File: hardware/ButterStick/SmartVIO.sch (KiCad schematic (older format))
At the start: 3 parts, among them U19 ATmega328PB-MU

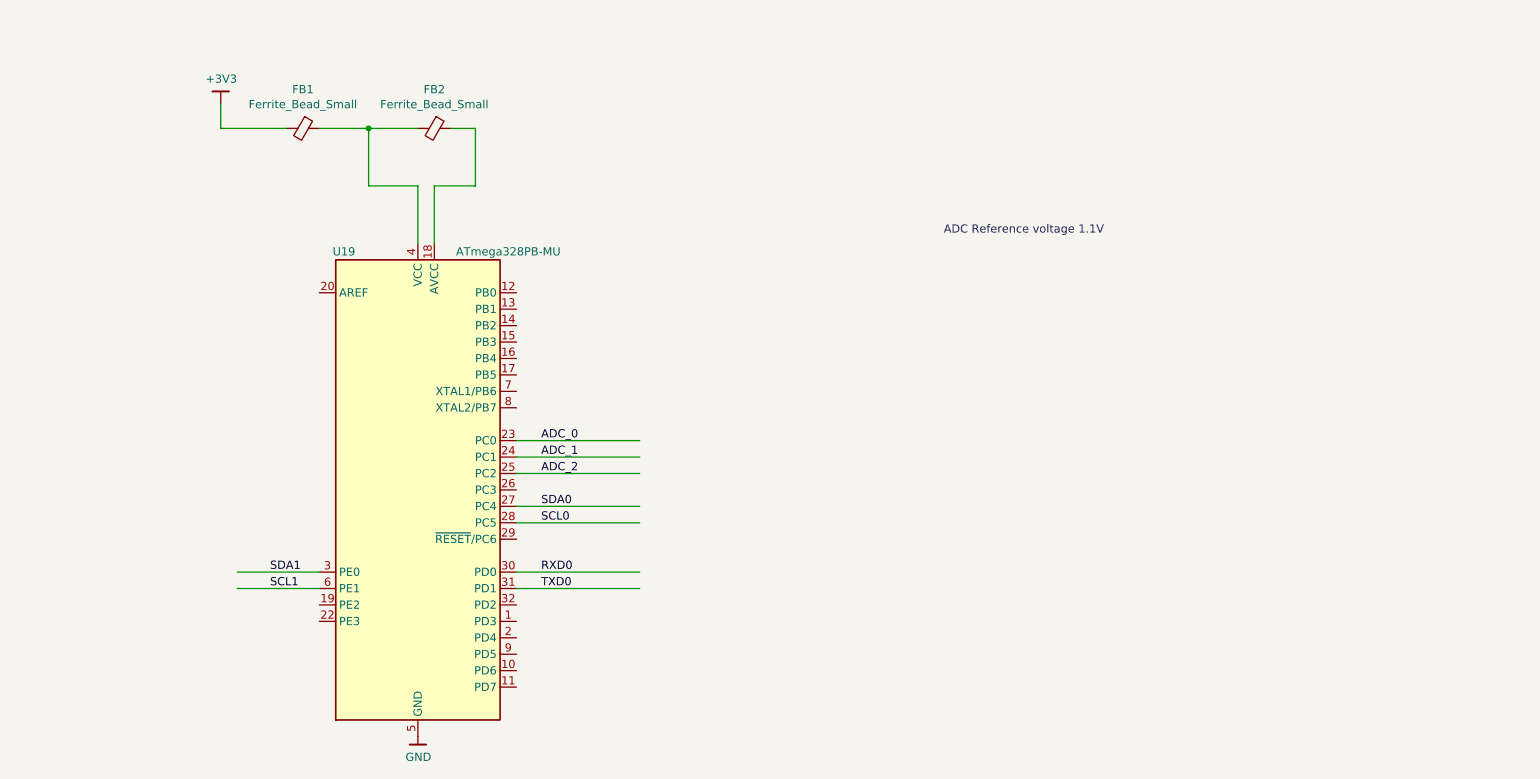
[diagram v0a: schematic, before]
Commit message: Added ESD on SD card signals.
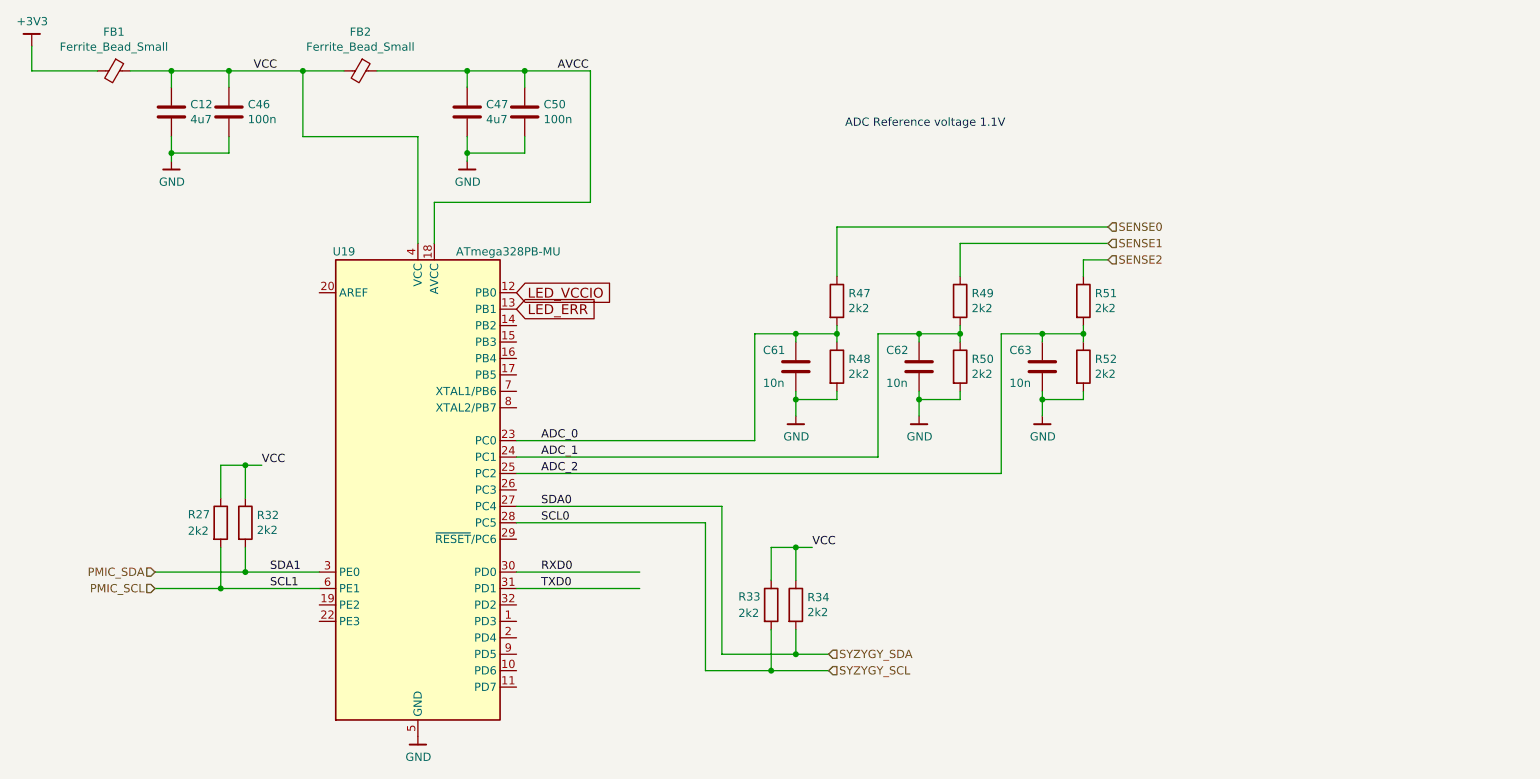
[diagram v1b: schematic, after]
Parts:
- added C12, C47: 4u7, pkl_dipol:C_0603, symbol Device:C
- added C46, C50: 100n, pkl_dipol:C_0402, symbol Device:C
- added C61, C62, C63: 10n, pkl_dipol:C_0402, symbol Device:C
- added R27, R32, R33, R34, R47, R48, R49, R50, R51, R52: 2k2, pkl_dipol:R_0402, symbol Device:R
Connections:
- net labels added: AVCC, LED_ERR, LED_VCCIO, PMIC_SCL, PMIC_SDA, SENSE0, SENSE1, SENSE2, SYZYGY_SCL, SYZYGY_SDA, VCC
- wire segments 20 -> 92
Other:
- moved on the sheet: FB1, FB2

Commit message: Update KiCad PCB.
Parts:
- added C71: 100n, pkl_dipol:C_0402, symbol Device:C
- added J7: TagConnect, pkl_tag_connect:TC2030-NL_SMALL, symbol Connector_Generic:Conn_02x03_Odd_Even
- added R60: 2k2, pkl_dipol:R_0402, symbol Device:R
- added Y2: Resonator, Crystal:Resonator_SMD_muRata_CSTxExxV-3Pin_3.0x1.1mm, symbol Device:Resonator
- U19: MFG (none) -> Microchip Technology; PN (none) -> ATMEGA328PB-MUR
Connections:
- net GND: now also C71.2, J7.6 (Pin_6), Y2.2
- net VCC: now also J7.2 (Pin_2), R60.1
- net EN1: now reaches U19.10 (PD6)
- net EN2: now reaches U19.11 (PD7)
- net MOSI: now reaches U19.15 (PB3)
- net MOSI: now also J7.4 (Pin_4)
- net MISO: now reaches U19.16 (PB4)
- net MISO: now also J7.1 (Pin_1)
- net SCK: now reaches U19.17 (PB5)
- net SCK: now also J7.3 (Pin_3)
- net at U19.20 (AREF): now also C71.1
- net RESET: now reaches U19.29 (~RESET~/PC6)
- net RESET: now also J7.5 (Pin_5), R60.2
- net at U19.7 (XTAL1/PB6): now also Y2.1
- net at U19.8 (XTAL2/PB7): now also Y2.3
- net EN0: now reaches U19.9 (PD5)
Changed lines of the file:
@@
 F 2 "Package_DFN_QFN:QFN-32-1EP_5x5mm_P0.5mm_EP3.1x3.1mm" H 3650 3950 50  0001 C CIN
 F 3 "http://ww1.microchip.com/downloads/en/DeviceDoc/40001906C.pdf" H 3650 3950 50  0001 C CNN
+F 4 "Microchip Technology" H 0   0   50  0001 C CNN "MFG"
+F 5 "ATMEGA328PB-MUR" H 0   0   50  0001 C CNN "PN"
 	1    3650 3950
 	1    0    0    -1
@@
 Text GLabel 4250 2850 2    60   Input ~ 0
 LED_ERR
+Text HLabel 4250 4950 2    50   Input ~ 0
+EN0
+Text HLabel 4250 5050 2    50   Input ~ 0
+EN1
+Text HLabel 4250 5150 2    50   Input ~ 0
+EN2
+$Comp
+L Device:C C71
+U 1 1 5CF01D14
+P 2700 3000
+F 0 "C71" H 2815 3046 50  0000 L CNN
+F 1 "100n" H 2815 2955 50  0000 L CNN
+F 2 "pkl_dipol:C_0402" H 2738 2850 50  0001 C CNN
+F 3 "~" H 2700 3000 50  0001 C CNN
+	1    2700 3000
+	1    0    0    -1
+$EndComp
+$Comp
+L gkl_power:GND #PWR0269
+U 1 1 5CF01D9A
+P 2700 3250
+F 0 "#PWR0269" H 2700 3000 50  0001 C CNN
+F 1 "GND" H 2703 3124 50  0000 C CNN
+F 2 "" H 2600 2900 50  0001 C CNN
+F 3 "" H 2700 3250 50  0001 C CNN
+	1    2700 3250
+	1    0    0    -1
+$EndComp
+Wire Wire Line
+	2700 3250 2700 3150
+Wire Wire Line
+	2700 2850 2700 2750
+Wire Wire Line
+	2700 2750 3050 2750
+$Comp
+L Device:Resonator Y2
+U 1 1 5CF061F0
+P 5300 2700
+F 0 "Y2" H 5300 2948 50  0000 C CNN
+F 1 "Resonator" H 5300 2857 50  0000 C CNN
+F 2 "Crystal:Resonator_SMD_muRata_CSTxExxV-3Pin_3.0x1.1mm" H 5275 2700 50  0001 C CNN
+F 3 "~" H 5275 2700 50  0001 C CNN
+F 4 "Murata Electronics North America" H 5300 2700 50  0001 C CNN "MFG"
+F 5 "CSTCE8M00G52-R0" H 5300 2700 50  0001 C CNN "PN"
+	1    5300 2700
+	1    0    0    -1
+$EndComp
+Wire Wire Line
+	4250 3350 5050 3350
+Wire Wire Line
+	5050 3350 5050 2700
+Wire Wire Line
+	5050 2700 5150 2700
+Wire Wire Line
+	5450 2700 5550 2700
+Wire Wire Line
+	5550 2700 5550 3450
+Wire Wire Line
+	5550 3450 4250 3450
+Wire Wire Line
+	5300 2900 5300 3000
+$Comp
+L gkl_power:GND #PWR0270
+U 1 1 5CF0D6F1
+P 5300 3000
+F 0 "#PWR0270" H 5300 2750 50  0001 C CNN
+F 1 "GND" H 5303 2874 50  0000 C CNN
+F 2 "" H 5200 2650 50  0001 C CNN
+F 3 "" H 5300 3000 50  0001 C CNN
+	1    5300 3000
+	1    0    0    -1
+$EndComp
+Wire Wire Line
+	4250 3250 4600 3250
+Text Label 4600 3250 2    50   ~ 0
+SCK
+Wire Wire Line
+	4250 3150 4600 3150
+Text Label 4600 3150 2    50   ~ 0
+MISO
+Wire Wire Line
+	4250 3050 4600 3050
+Text Label 4600 3050 2    50   ~ 0
+MOSI
+Wire Wire Line
+	4250 4250 4600 4250
+Text Label 4600 4250 2    50   ~ 0
+RESET
+$Comp
+L Connector_Generic:Conn_02x03_Odd_Even J7
+U 1 1 5CF73B2A
+P 9650 4000
+F 0 "J7" H 9700 4317 50  0000 C CNN
+F 1 "TagConnect" H 9700 4226 50  0000 C CNN
+F 2 "pkl_tag_connect:TC2030-NL_SMALL" H 9650 4000 50  0001 C CNN
+F 3 "~" H 9650 4000 50  0001 C CNN
+	1    9650 4000
+	1    0    0    -1
+$EndComp
+Wire Wire Line
+	9450 3900 9000 3900
+Wire Wire Line
+	9450 4000 9000 4000
+Wire Wire Line
+	9450 4100 9000 4100
+Wire Wire Line
+	10100 3900 9950 3900
+Wire Wire Line
+	10400 4000 9950 4000
+Wire Wire Line
+	10100 4100 9950 4100
+Wire Wire Line
+	10100 3900 10100 3750
+Wire Wire Line
+	10100 4100 10100 4250
+$Comp
+L gkl_power:GND #PWR0271
+U 1 1 5CF85B49
+P 10100 4250
+F 0 "#PWR0271" H 10100 4000 50  0001 C CNN
+F 1 "GND" H 10103 4124 50  0000 C CNN
+F 2 "" H 10000 3900 50  0001 C CNN
+F 3 "" H 10100 4250 50  0001 C CNN
+	1    10100 4250
+	1    0    0    -1
+$EndComp
+Text Label 10100 3750 0    50   ~ 0
+VCC
+Text Label 9000 4100 0    50   ~ 0
+RESET
+Text Label 9000 4000 0    50   ~ 0
+SCK
+Text Label 9000 3900 0    50   ~ 0
+MISO
+Text Label 10400 4000 2    50   ~ 0
+MOSI
+Text Label 9350 3400 2    50   ~ 0
+RESET
+Wire Wire Line
+	9350 3400 9650 3400
+Wire Wire Line
+	9650 3400 9650 3050
+$Comp
+L Device:R R60
+U 1 1 5CF89112
+P 9650 2900
+F 0 "R60" H 9720 2946 50  0000 L CNN
+F 1 "2k2" H 9720 2855 50  0000 L CNN
+F 2 "pkl_dipol:R_0402" V 9580 2900 50  0001 C CNN
+F 3 "~" H 9650 2900 50  0001 C CNN
+	1    9650 2900
+	1    0    0    -1
+$EndComp
+Text Label 9750 2550 0    50   ~ 0
+VCC
+Wire Wire Line
+	9650 2750 9650 2550
+Wire Wire Line
+	9650 2550 9750 2550
 $EndSCHEMATC
